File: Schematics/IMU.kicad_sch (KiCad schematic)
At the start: 4 parts, among them U7 LSM6DS3TR-C

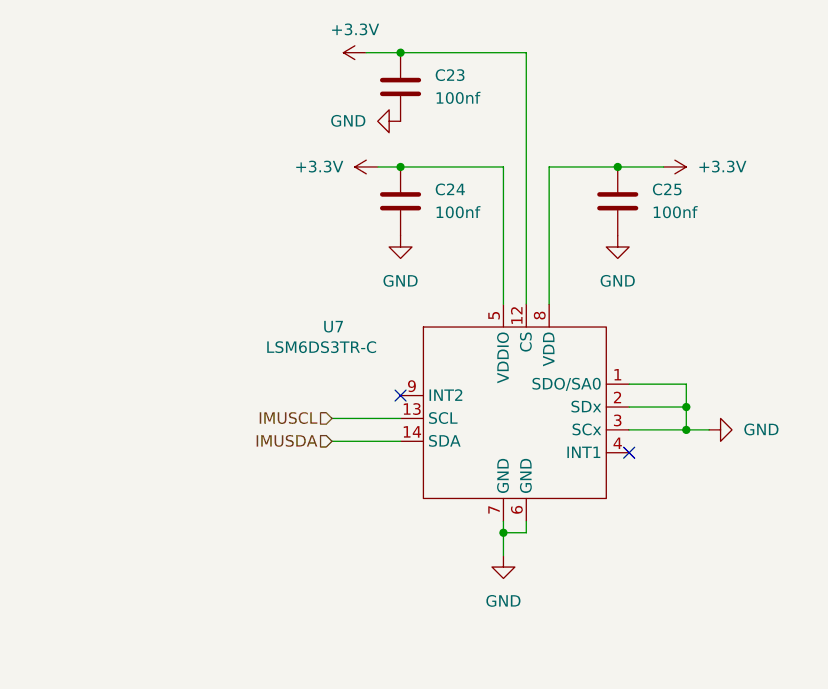
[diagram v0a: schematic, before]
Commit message: added aux pyro added reverse polarity protection re routed just need to clean up and check pin assignments
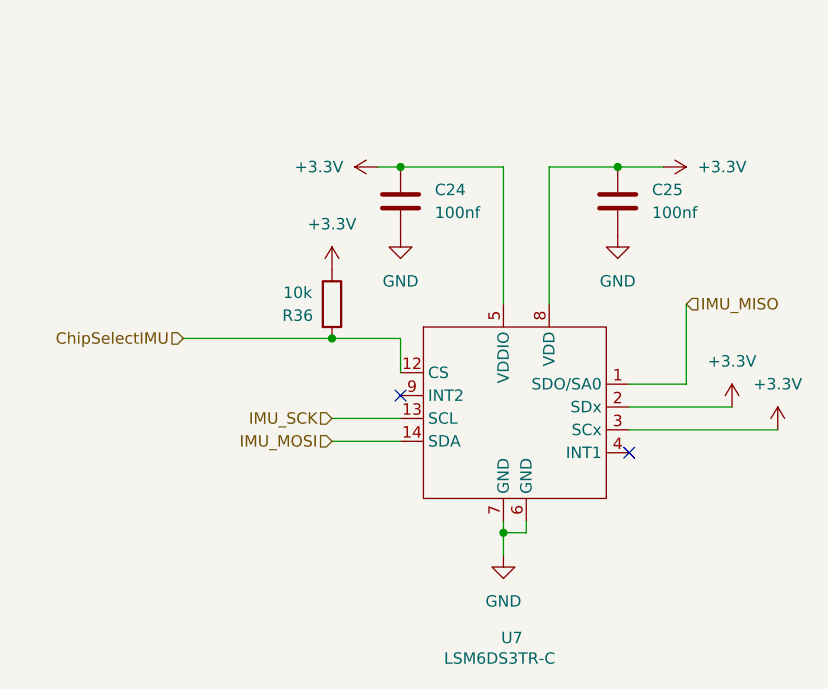
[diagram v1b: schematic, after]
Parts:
- removed C23: 100nf, Capacitor_SMD:C_0805_2012Metric_Pad1.18x1.45mm_HandSolder, symbol Device:C
- added R36: 10k, Resistor_SMD:R_0805_2012Metric_Pad1.20x1.40mm_HandSolder, symbol Device:R
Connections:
- net +3.3V: now also U7.2 (SDx), U7.3 (SCx), R36.1; no longer U7.12 (CS)
- net GND: no longer U7.1 (SDO/SA0), U7.2 (SDx), U7.3 (SCx)
- net IMUSCL renamed IMU_SCK
- net IMUSDA renamed IMU_MOSI
- new net ChipSelectIMU: R36.2, U7.12 (CS)
- new net IMU_MISO: U7.1 (SDO/SA0)
